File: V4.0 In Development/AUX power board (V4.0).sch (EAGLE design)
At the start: 96 parts, among them U1 ATMEGA328P_TQFP, U2 TPS5405DR

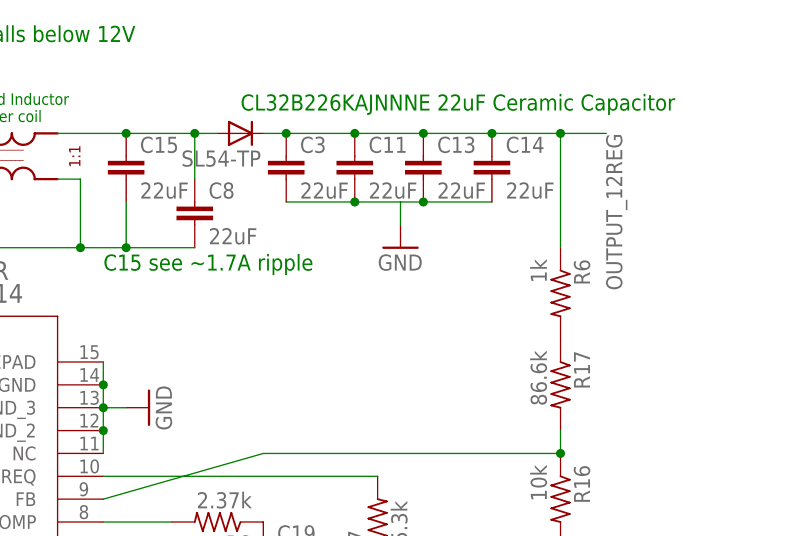
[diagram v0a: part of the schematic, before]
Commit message: Generated the board file
-Generated Board files
-Sorted the components
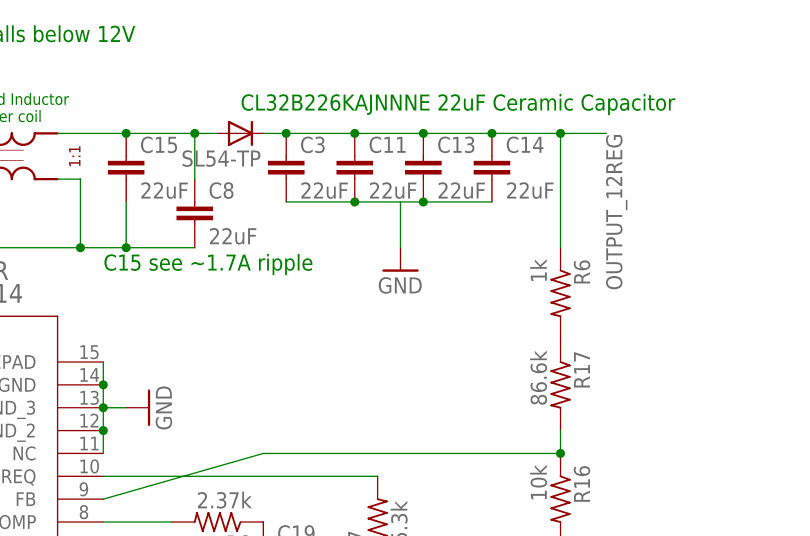
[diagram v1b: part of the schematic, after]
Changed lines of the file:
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@@
 <instance part="C14" gate="G$1" x="170.18" y="228.6"/>
 <instance part="C15" gate="G$1" x="129.54" y="228.6"/>
-<instance part="GND1" gate="1" x="160.02" y="218.44"/>
+<instance part="GND1" gate="1" x="160.02" y="215.9"/>
 <instance part="GND2" gate="1" x="99.06" y="231.14" rot="R270"/>
 <instance part="SL54-TP" gate="G$1" x="142.24" y="231.14" rot="R90"/>
@@
 <wire x1="170.18" y1="223.52" x2="162.56" y2="223.52" width="0.1524" layer="91"/>
 <junction x="162.56" y="223.52"/>
-<wire x1="160.02" y1="223.52" x2="160.02" y2="220.98" width="0.1524" layer="91"/>
+<wire x1="160.02" y1="223.52" x2="160.02" y2="218.44" width="0.1524" layer="91"/>
 <pinref part="GND1" gate="1" pin="GND"/>
 <pinref part="C11" gate="G$1" pin="2"/>

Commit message: Worked on PCB (Input)
-Not complete
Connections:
- net GND: no longer U$10.SH1, U$10.SH2, U$3.SH1, U$3.SH2, U$4.SH1, U$4.SH2
- net NEG_TERMINAL: now also U$10.SH1, U$10.SH2, U$3.SH1, U$3.SH2, U$4.SH1, U$4.SH2
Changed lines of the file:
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@@
-</segment>
-<segment>
-<pinref part="U$3" gate="G$1" pin="SH1"/>
-<wire x1="228.6" y1="-5.08" x2="226.06" y2="-5.08" width="0.1524" layer="91"/>
-<label x="220.98" y="-5.08" size="1.778" layer="95"/>
-</segment>
-<segment>
-<pinref part="U$3" gate="G$1" pin="SH2"/>
-<wire x1="228.6" y1="-10.16" x2="226.06" y2="-10.16" width="0.1524" layer="91"/>
-<label x="220.98" y="-10.16" size="1.778" layer="95"/>
 </segment>
 <segment>
@@
 </segment>
 <segment>
-<pinref part="U$4" gate="G$1" pin="SH1"/>
-<wire x1="264.16" y1="-5.08" x2="261.62" y2="-5.08" width="0.1524" layer="91"/>
-<label x="256.54" y="-5.08" size="1.778" layer="95"/>
-</segment>
-<segment>
-<pinref part="U$4" gate="G$1" pin="SH2"/>
-<wire x1="264.16" y1="-10.16" x2="261.62" y2="-10.16" width="0.1524" layer="91"/>
-<label x="256.54" y="-10.16" size="1.778" layer="95"/>
-</segment>
-<segment>
 <wire x1="264.16" y1="25.4" x2="261.62" y2="25.4" width="0.1524" layer="91"/>
 <label x="256.54" y="25.4" size="1.778" layer="95"/>
@@
 <wire x1="264.16" y1="0" x2="261.62" y2="0" width="0.1524" layer="91"/>
 <label x="256.54" y="0" size="1.778" layer="95"/>
-</segment>
-<segment>
-<pinref part="U$10" gate="G$1" pin="SH1"/>
-<wire x1="299.72" y1="-5.08" x2="297.18" y2="-5.08" width="0.1524" layer="91"/>
-<label x="292.1" y="-5.08" size="1.778" layer="95"/>
-</segment>
-<segment>
-<pinref part="U$10" gate="G$1" pin="SH2"/>
-<wire x1="299.72" y1="-10.16" x2="297.18" y2="-10.16" width="0.1524" layer="91"/>
-<label x="292.1" y="-10.16" size="1.778" layer="95"/>
 </segment>
 <segment>
@@
 <label x="81.28" y="-12.7" size="1.778" layer="95"/>
 </segment>
-</net>
+<segment>
+<pinref part="U$3" gate="G$1" pin="SH1"/>
+<wire x1="228.6" y1="-5.08" x2="226.06" y2="-5.08" width="0.1524" layer="91"/>
+<label x="220.98" y="-5.08" size="1.778" layer="95"/>
+</segment>
+<segment>
+<pinref part="U$3" gate="G$1" pin="SH2"/>
+<wire x1="228.6" y1="-10.16" x2="226.06" y2="-10.16" width="0.1524" layer="91"/>
+<label x="220.98" y="-10.16" size="1.778" layer="95"/>
+</segment>
+<segment>
+<pinref part="U$4" gate="G$1" pin="SH1"/>
+<wire x1="264.16" y1="-5.08" x2="261.62" y2="-5.08" width="0.1524" layer="91"/>
+<label x="256.54" y="-5.08" size="1.778" layer="95"/>
+</segment>
+<segment>
+<pinref part="U$4" gate="G$1" pin="SH2"/>
+<wire x1="264.16" y1="-10.16" x2="261.62" y2="-10.16" width="0.1524" layer="91"/>
+<label x="256.54" y="-10.16" size="1.778" layer="95"/>
+</segment>
+<segment>
+<pinref part="U$10" gate="G$1" pin="SH1"/>
+<wire x1="299.72" y1="-5.08" x2="297.18" y2="-5.08" width="0.1524" layer="91"/>
+<label x="292.1" y="-5.08" size="1.778" layer="95"/>
+</segment>
+<segment>
+<pinref part="U$10" gate="G$1" pin="SH2"/>
+<wire x1="299.72" y1="-10.16" x2="297.18" y2="-10.16" width="0.1524" layer="91"/>
+<label x="292.1" y="-10.16" size="1.778" layer="95"/>
+</segment>
+</net>

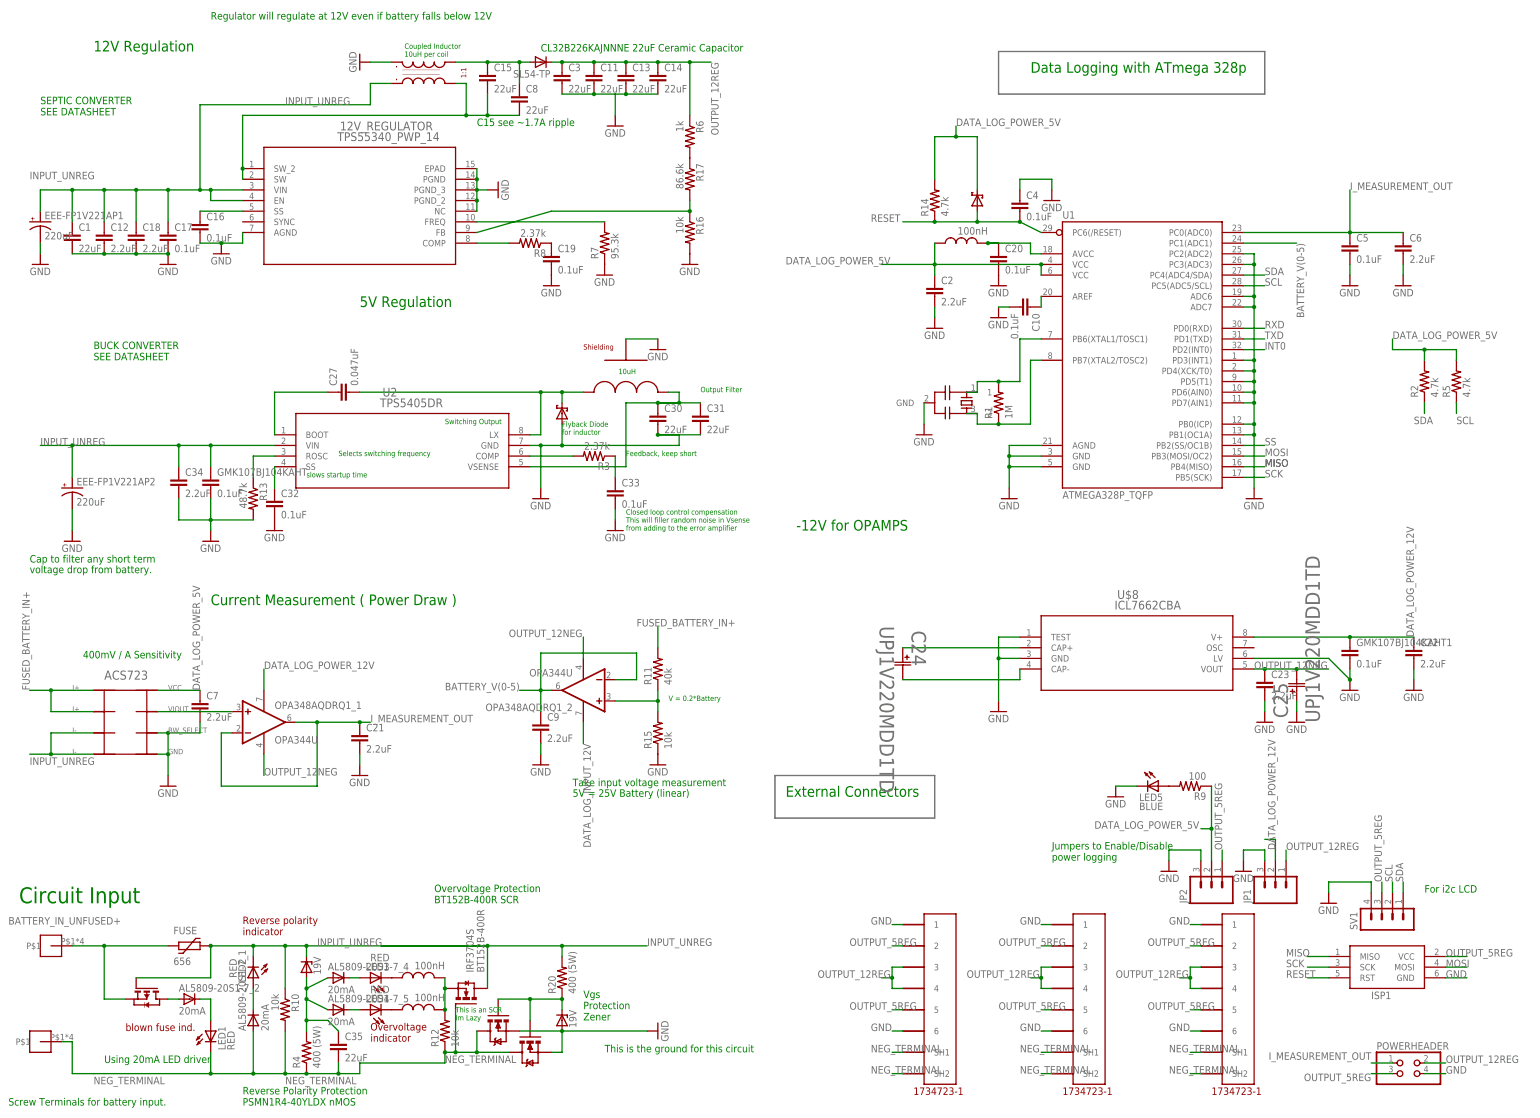
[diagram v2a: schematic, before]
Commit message: Deleted -12V REG and op-amps
They add complexity/expense/risk without adding much performance.

When testing the -12V on the motor controller, the performance was poor. I am too lazy to re-spec a part so its much more efficient on time to just remove it.
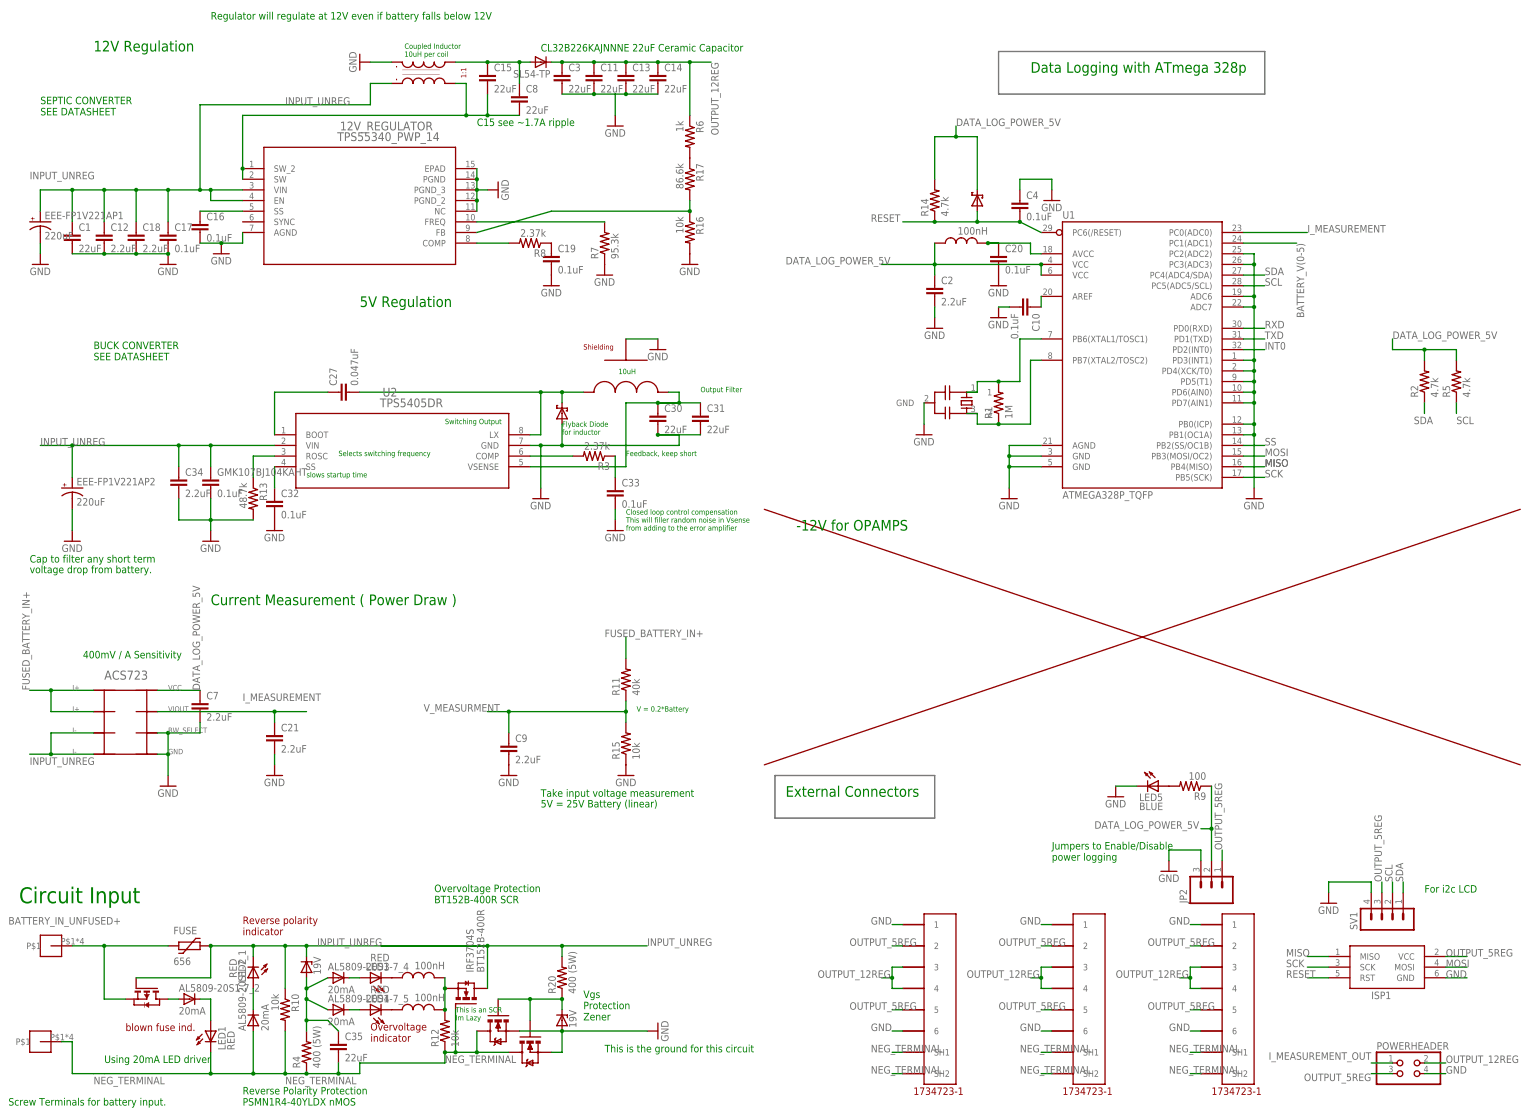
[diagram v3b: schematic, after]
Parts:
- removed C22, C23, C6: 2.2uF, rcl:C-EUC0603
- removed C24, C25: UPJ1V220MDD1TD, UPJ1V220MDD1TD:UPJ1V220MDD1TD
- removed C5, GMK107BJ104KAHT1: 0.1uF, rcl:C-EUC0603
- removed JP1: (no value), SparkFun (2015_10_14 22_27_04 UTC):M03PTH
- removed OPA348AQDRQ1_1, OPA348AQDRQ1_2: OPA344U, linear:OPA344U
- removed U$8: ICL7662CBA, linear:ICL7662CBA
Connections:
- removed net DATA_LOG_INPUT_12V: OPA348AQDRQ1_2.V+
- removed net DATA_LOG_POWER_12V: C22.1, GMK107BJ104KAHT1.1, JP1.2, OPA348AQDRQ1_1.V+, U$8.V+
- removed net N$11: C24.22, U$8.CAP-
- removed net N$12: OPA348AQDRQ1_2.+IN, R11.1, R15.2
- removed net N$16: C24.11, U$8.CAP+
- removed net N$2: OPA348AQDRQ1_1.+IN, U$1.P$7
- removed net OUTPUT_12NEG: C23.1, C25.22, OPA348AQDRQ1_1.V-, OPA348AQDRQ1_2.V-, U$8.VOUT
- new net I_MEASUREMENT: C21.1, U$1.P$7, U1.PC0(ADC0)
- new net V_MEASURMENT: C9.1, R11.1, R15.2
- net BATTERY_V(0-5): no longer C9.1, OPA348AQDRQ1_2.-IN, OPA348AQDRQ1_2.OUT
- net GND: no longer C22.2, C25.11, C5.2, C6.2, GMK107BJ104KAHT1.2, JP1.3, U$8.GND, U$8.LV, U$8.TEST
- net I_MEASUREMENT_OUT: no longer C21.1, C5.1, C6.1, OPA348AQDRQ1_1.-IN, OPA348AQDRQ1_1.OUT, U1.PC0(ADC0)
- net OUTPUT_12REG: no longer JP1.1
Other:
- moved on the sheet: C21, C9, R11, R15
